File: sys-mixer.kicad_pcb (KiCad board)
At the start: 2 copper layers, 122 x 84 mm, 16 parts, among them J1 RCA L&R, J2 RCA L&R, J3 RCA L&R, SW1 4PDT

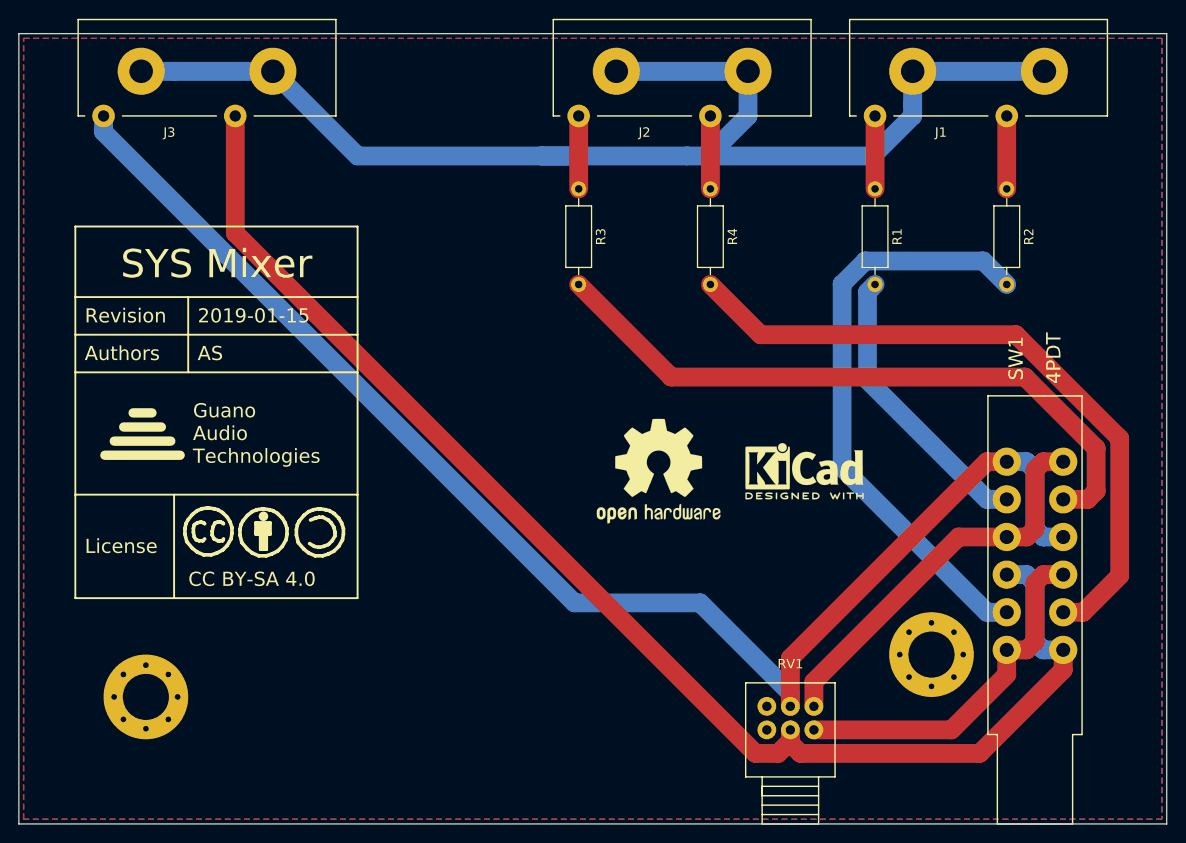
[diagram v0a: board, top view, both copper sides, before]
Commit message: Add github URL to silkscreen
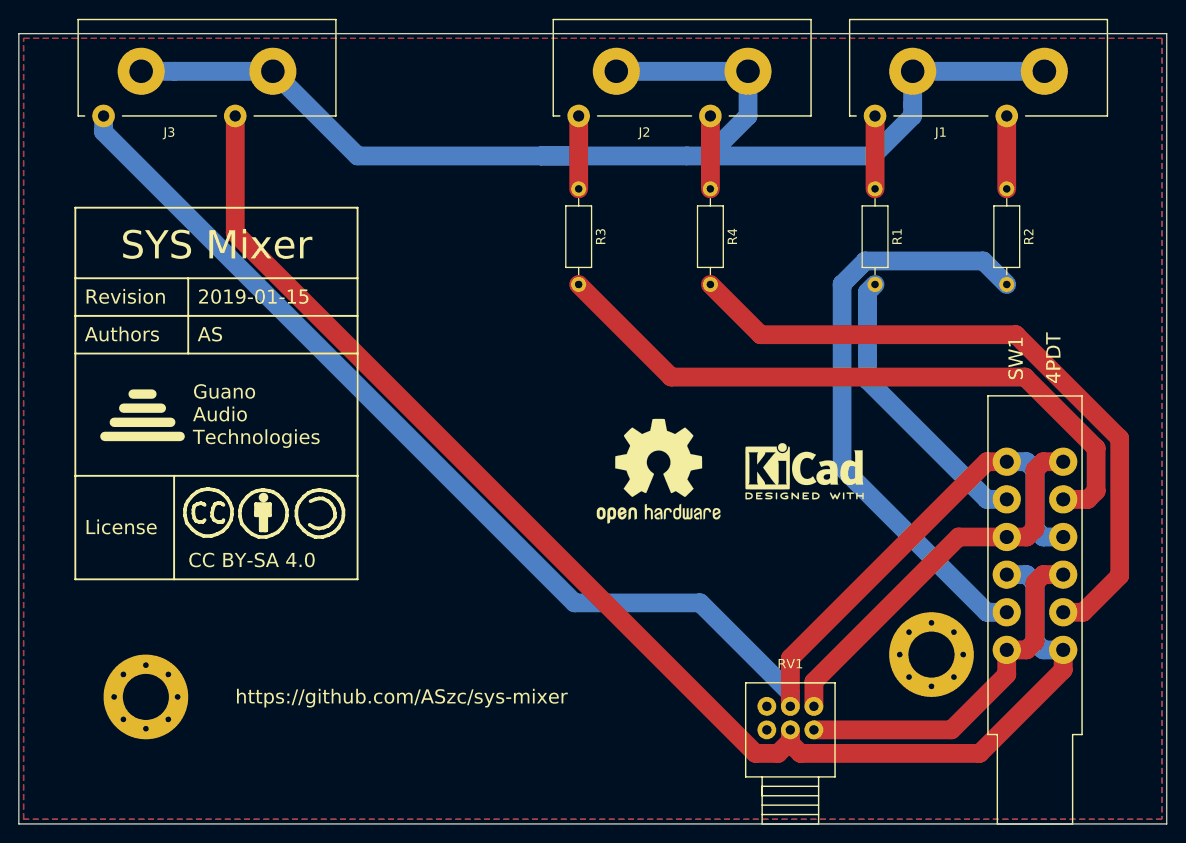
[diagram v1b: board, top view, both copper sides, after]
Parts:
- moved ? 2.00 mm to (70.0, 76.0)
- moved ? 2.00 mm to (76.0, 76.0)
- moved ? 2.00 mm to (82.0, 76.0)
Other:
- board text added: "https://github.com/ASzc/sys-mixer"
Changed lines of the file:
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@@
   (general
     (thickness 1.6)
-    (drawings 28)
+    (drawings 29)
     (tracks 88)
     (zones 0)
@@
   )
   (module extra-footprints:Symbol_CreativeCommons_Silkscreen_Type2_Small (layer F.Cu)
-    (at 70 78)
+    (at 70 76)
     (descr "Symbol, Creative Commons, Silkscreen, Type 2, Small,")
     (tags "Symbol, Creative Commons, Silkscreen, Type 2, Small,")
@@
   )
   (module extra-footprints:Symbol_CC-Attribution_Silkscreen_Small (layer F.Cu)
-    (at 76 78)
+    (at 76 76)
     (descr "Symbol, CC-Share Alike, Silkscreen, Small,")
     (tags "Symbol, CC-Share Alike, Silkscreen, Small,")
@@
   )
   (module extra-footprints:Symbol_CC-ShareAlike_Silkscreen_Small (layer F.Cu)
-    (at 82 78)
+    (at 82 76)
     (descr "Symbol, CC-Share Alike, Silkscreen, Small,")
     (tags "Symbol, CC-Share Alike, Silkscreen, Small,")
@@
     (fp_line (start -1.09982 1.19888) (end -0.59944 1.50114) (layer F.SilkS) (width 0.381))
   )
-  (gr_line (start 56 57) (end 86 57) (layer F.SilkS) (width 0.2))
-  (gr_line (start 56 61) (end 86 61) (layer F.SilkS) (width 0.2))
-  (gr_text Authors (at 57 59) (layer F.SilkS)
+  (gr_text https://github.com/ASzc/sys-mixer (at 73 95.5) (layer F.SilkS)
     (effects (font (size 1.5 1.5) (thickness 0.3)) (justify left))
   )
-  (gr_text AS (at 69 59) (layer F.SilkS)
+  (gr_line (start 56 55) (end 86 55) (layer F.SilkS) (width 0.2))
+  (gr_line (start 56 59) (end 86 59) (layer F.SilkS) (width 0.2))
+  (gr_text Authors (at 57 57) (layer F.SilkS)
     (effects (font (size 1.5 1.5) (thickness 0.3)) (justify left))
   )
-  (gr_text "CC BY-SA 4.0" (at 68 83) (layer F.SilkS)
+  (gr_text AS (at 69 57) (layer F.SilkS)
     (effects (font (size 1.5 1.5) (thickness 0.3)) (justify left))
   )
-  (gr_line (start 66.5 74) (end 66.5 85) (layer F.SilkS) (width 0.2))
-  (gr_line (start 86 85) (end 86 74) (layer F.SilkS) (width 0.2))
-  (gr_line (start 56 85) (end 86 85) (layer F.SilkS) (width 0.2))
-  (gr_line (start 56 74) (end 56 85) (layer F.SilkS) (width 0.2))
-  (gr_text License (at 57 79.5) (layer F.SilkS)
+  (gr_text "CC BY-SA 4.0" (at 68 81) (layer F.SilkS)
     (effects (font (size 1.5 1.5) (thickness 0.3)) (justify left))
   )
-  (gr_line (start 68 53) (end 68 61) (layer F.SilkS) (width 0.2))
-  (gr_line (start 86 53) (end 56 53) (layer F.SilkS) (width 0.2))
-  (gr_line (start 86 45.5) (end 56 45.5) (layer F.SilkS) (width 0.2))
-  (gr_line (start 86 74) (end 86 45.5) (layer F.SilkS) (width 0.2))
-  (gr_line (start 56 74) (end 86 74) (layer F.SilkS) (width 0.2))
-  (gr_line (start 56 45.5) (end 56 74) (layer F.SilkS) (width 0.2))
-  (gr_text 2019-01-15 (at 69 55) (layer F.SilkS)
+  (gr_line (start 66.5 72) (end 66.5 83) (layer F.SilkS) (width 0.2))
+  (gr_line (start 86 83) (end 86 72) (layer F.SilkS) (width 0.2))
+  (gr_line (start 56 83) (end 86 83) (layer F.SilkS) (width 0.2))
+  (gr_line (start 56 72) (end 56 83) (layer F.SilkS) (width 0.2))
+  (gr_text License (at 57 77.5) (layer F.SilkS)
     (effects (font (size 1.5 1.5) (thickness 0.3)) (justify left))
   )
-  (gr_text Revision (at 57 55) (layer F.SilkS)
+  (gr_line (start 68 51) (end 68 59) (layer F.SilkS) (width 0.2))
+  (gr_line (start 86 51) (end 56 51) (layer F.SilkS) (width 0.2))
+  (gr_line (start 86 43.5) (end 56 43.5) (layer F.SilkS) (width 0.2))
+  (gr_line (start 86 72) (end 86 43.5) (layer F.SilkS) (width 0.2))
+  (gr_line (start 56 72) (end 86 72) (layer F.SilkS) (width 0.2))
+  (gr_line (start 56 43.5) (end 56 72) (layer F.SilkS) (width 0.2))
+  (gr_text 2019-01-15 (at 69 53) (layer F.SilkS)
     (effects (font (size 1.5 1.5) (thickness 0.3)) (justify left))
   )
-  (gr_text "SYS Mixer" (at 71 49.5) (layer F.SilkS)
+  (gr_text Revision (at 57 53) (layer F.SilkS)
+    (effects (font (size 1.5 1.5) (thickness 0.3)) (justify left))
+  )
+  (gr_text "SYS Mixer" (at 71 47.5) (layer F.SilkS)
     (effects (font (size 3 3) (thickness 0.5)))
   )
-  (gr_line (start 64.142965 65.310602) (end 62.142965 65.310602) (layer F.SilkS) (width 1))
-  (gr_line (start 65.142965 66.810602) (end 61.142965 66.810602) (layer F.SilkS) (width 1))
-  (gr_line (start 66.142965 68.310602) (end 60.142965 68.310602) (layer F.SilkS) (width 1))
-  (gr_line (start 67.142965 69.810602) (end 59.142965 69.810602) (layer F.SilkS) (width 1))
-  (gr_text "Guano\nAudio\nTechnologies" (at 68.5 67.5) (layer F.SilkS)
+  (gr_line (start 64.142965 63.310602) (end 62.142965 63.310602) (layer F.SilkS) (width 1))
+  (gr_line (start 65.142965 64.810602) (end 61.142965 64.810602) (layer F.SilkS) (width 1))
+  (gr_line (start 66.142965 66.310602) (end 60.142965 66.310602) (layer F.SilkS) (width 1))
+  (gr_line (start 67.142965 67.810602) (end 59.142965 67.810602) (layer F.SilkS) (width 1))
+  (gr_text "Guano\nAudio\nTechnologies" (at 68.5 65.5) (layer F.SilkS)
     (effects (font (size 1.5 1.5) (thickness 0.3)) (justify left))
   )
@@
   (gr_line (start 172 25) (end 172 109) (layer Edge.Cuts) (width 0.01))
   (gr_line (start 50 25) (end 172 25) (layer Edge.Cuts) (width 0.01))
-  (segment (start 66.535533 29) (end 77 29) (width 2) (layer B.Cu) (net 13))
-  (segment (start 63 29) (end 66.535533 29) (width 2) (layer B.Cu) (net 13))
-  (segment (start 77 29) (end 86 38) (width 2) (layer B.Cu) (net 13))
-  (segment (start 145 32.535533) (end 145 29) (width 2) (layer B.Cu) (net 13))
-  (segment (start 145 33.746002) (end 145 32.535533) (width 2) (layer B.Cu) (net 13))
-  (segment (start 140.746002 38) (end 145 33.746002) (width 2) (layer B.Cu) (net 13))
-  (segment (start 123.246002 38) (end 140.746002 38) (width 2) (layer B.Cu) (net 13))
-  (segment (start 113.5 29) (end 127.5 29) (width 2) (layer B.Cu) (net 13))
-  (segment (start 145 29) (end 159 29) (width 2) (layer B.Cu) (net 13))
-  (segment (start 109.246002 38) (end 105.5 38) (width 2) (layer B.Cu) (net 13))
-  (segment (start 123.246002 38) (end 121 38) (width 2) (layer B.Cu) (net 13))
-  (segment (start 127.5 29) (end 127.5 33.746002) (width 2) (layer B.Cu) (net 13))
-  (segment (start 127.5 33.746002) (end 123.246002 38) (width 2) (layer B.Cu) (net 13))
-  (segment (start 105.5 38) (end 121 38) (width 2) (layer B.Cu) (net 13))
   (segment (start 141 33.75) (end 141 41.5) (width 2) (layer F.Cu) (net 1))
   (segment (start 155 33.75) (end 155 41.5) (width 2) (layer F.Cu) (net 2))
@@
   (segment (start 152.499991 49.159991) (end 139.964461 49.159991) (width 2) (layer B.Cu) (net 8))
   (segment (start 155 51.66) (end 152.499991 49.159991) (width 2) (layer B.Cu) (net 8))
-  (segment (start 161.059998 86.5) (end 161.5 86.5) (width 2) (layer F.Cu) (net 10))
   (segment (start 161.059998 74.5) (end 161.5 74.5) (width 2) (layer B.Cu) (net 9))
   (segment (start 164.500001 69.059999) (end 164.500001 73.621319) (width 2) (layer F.Cu) (net 9))
@@
   (segment (start 163.62132 74.5) (end 161 74.5) (width 2) (layer F.Cu) (net 9))
   (segment (start 164.500001 73.621319) (end 163.62132 74.5) (width 2) (layer F.Cu) (net 9))
+  (segment (start 161.059998 86.5) (end 161.5 86.5) (width 2) (layer F.Cu) (net 10))
   (segment (start 163.12132 86.5) (end 161 86.5) (width 2) (layer F.Cu) (net 10))
   (segment (start 167.000011 82.621309) (end 163.12132 86.5) (width 2) (layer F.Cu) (net 10))
@@
   (segment (start 158 77.62132) (end 158 71.37868) (width 2) (layer F.Cu) (net 12))
   (segment (start 155 78.5) (end 157.12132 78.5) (width 2) (layer F.Cu) (net 12))
+  (segment (start 66.535533 29) (end 77 29) (width 2) (layer B.Cu) (net 13))
+  (segment (start 63 29) (end 66.535533 29) (width 2) (layer B.Cu) (net 13))
+  (segment (start 77 29) (end 86 38) (width 2) (layer B.Cu) (net 13))
+  (segment (start 145 32.535533) (end 145 29) (width 2) (layer B.Cu) (net 13))
+  (segment (start 145 33.746002) (end 145 32.535533) (width 2) (layer B.Cu) (net 13))
+  (segment (start 140.746002 38) (end 145 33.746002) (width 2) (layer B.Cu) (net 13))
+  (segment (start 123.246002 38) (end 140.746002 38) (width 2) (layer B.Cu) (net 13))
+  (segment (start 113.5 29) (end 127.5 29) (width 2) (layer B.Cu) (net 13))
+  (segment (start 145 29) (end 159 29) (width 2) (layer B.Cu) (net 13))
+  (segment (start 109.246002 38) (end 105.5 38) (width 2) (layer B.Cu) (net 13))
+  (segment (start 123.246002 38) (end 121 38) (width 2) (layer B.Cu) (net 13))
+  (segment (start 127.5 29) (end 127.5 33.746002) (width 2) (layer B.Cu) (net 13))
+  (segment (start 127.5 33.746002) (end 123.246002 38) (width 2) (layer B.Cu) (net 13))
+  (segment (start 105.5 38) (end 121 38) (width 2) (layer B.Cu) (net 13))
   (segment (start 86 38) (end 105.5 38) (width 2) (layer B.Cu) (net 13))
   (zone (net 13) (net_name "Net-(H1-Pad1)") (layer F.Cu) (hatch edge 0.508)

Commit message: Reroute output so both channels are on B.Cu
Also adjust silk info position
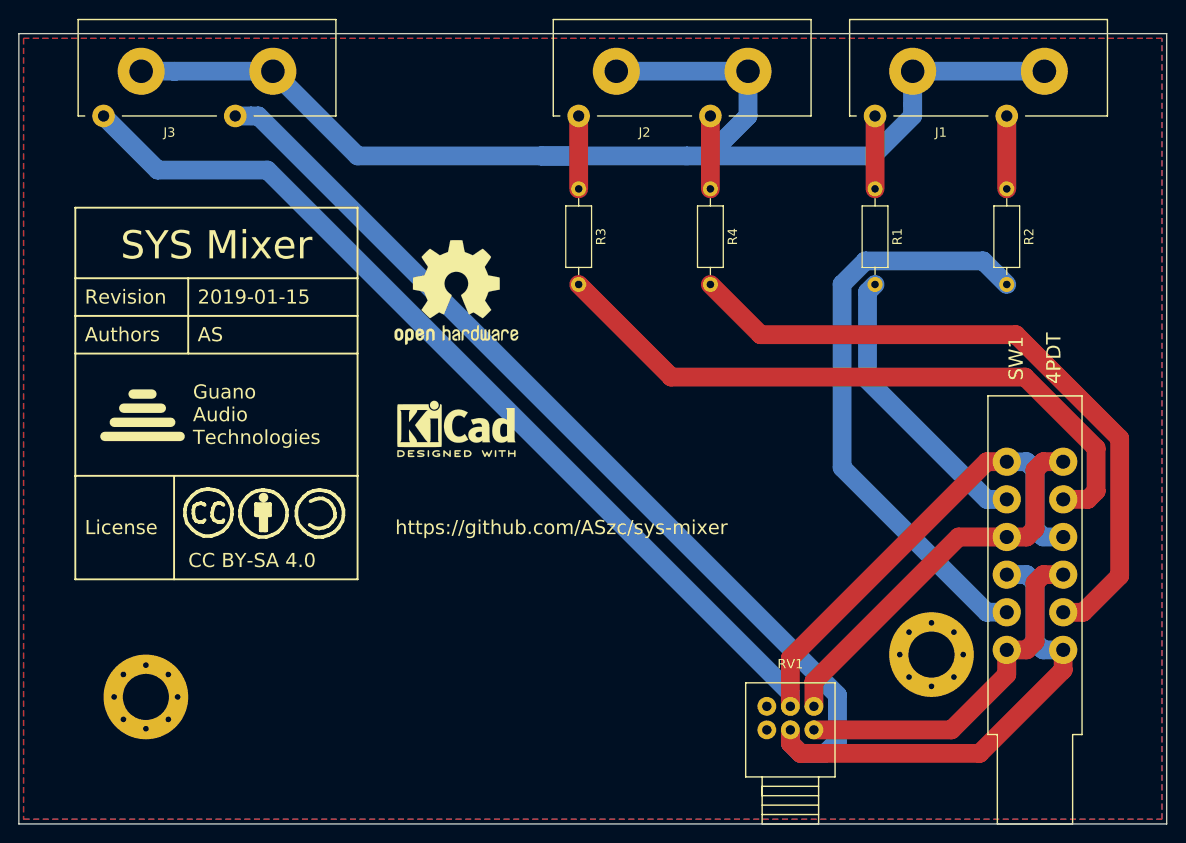
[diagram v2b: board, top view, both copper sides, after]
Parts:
- moved REF** 37.3 mm to (96.5, 67.0)
- moved REF** 28.7 mm to (96.5, 52.5)
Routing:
- net Net-(J3-Pad2): track 145.0 -> 151.9 mm
- net Net-(J3-Pad1): track 150.6 -> 149.6 mm
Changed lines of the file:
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@@
     (thickness 1.6)
     (drawings 29)
-    (tracks 88)
+    (tracks 91)
     (zones 0)
     (modules 16)
@@
   )
   (module Symbol:KiCad-Logo2_6mm_SilkScreen (layer F.Cu)
-    (at 133.5 71.5)
+    (at 96.5 67)
     (descr "KiCad Logo")
     (tags "Logo KiCad")
@@
   )
   (module Symbol:OSHW-Logo2_14.6x12mm_SilkScreen (layer F.Cu)
-    (at 118 71.5)
+    (at 96.5 52.5)
     (descr "Open Source Hardware Symbol")
     (tags "Logo Symbol OSHW")
@@
     (fp_line (start -1.09982 1.19888) (end -0.59944 1.50114) (layer F.SilkS) (width 0.381))
   )
-  (gr_text https://github.com/ASzc/sys-mixer (at 73 95.5) (layer F.SilkS)
+  (gr_text https://github.com/ASzc/sys-mixer (at 90 77.5) (layer F.SilkS)
     (effects (font (size 1.5 1.5) (thickness 0.3)) (justify left))
   )
@@
   (segment (start 123.5 33.75) (end 123.5 41.5) (width 2) (layer F.Cu) (net 3))
   (segment (start 109.5 33.75) (end 109.5 41.5) (width 2) (layer F.Cu) (net 4))
-  (segment (start 59 35.447056) (end 109.052944 85.5) (width 2) (layer B.Cu) (net 5))
-  (segment (start 59 33.75) (end 59 35.447056) (width 2) (layer B.Cu) (net 5))
   (segment (start 132 95.085787) (end 132 96.5) (width 2) (layer B.Cu) (net 5))
-  (segment (start 122.414213 85.5) (end 132 95.085787) (width 2) (layer B.Cu) (net 5))
-  (segment (start 109.052944 85.5) (end 122.414213 85.5) (width 2) (layer B.Cu) (net 5))
   (segment (start 152.87868 70.5) (end 155 70.5) (width 2) (layer F.Cu) (net 5))
   (segment (start 132 91.37868) (end 152.87868 70.5) (width 2) (layer F.Cu) (net 5))
@@
   (segment (start 158.87868 78.5) (end 158 77.62132) (width 2) (layer B.Cu) (net 5))
   (segment (start 161 78.5) (end 158.87868 78.5) (width 2) (layer B.Cu) (net 5))
-  (segment (start 130.700001 101.500001) (end 132 100.200002) (width 2) (layer F.Cu) (net 6))
-  (segment (start 128.299999 101.500001) (end 130.700001 101.500001) (width 2) (layer F.Cu) (net 6))
-  (segment (start 73 46.200002) (end 128.299999 101.500001) (width 2) (layer F.Cu) (net 6))
-  (segment (start 73 33.75) (end 73 46.200002) (width 2) (layer F.Cu) (net 6))
+  (segment (start 132 95.085787) (end 76.414213 39.5) (width 2) (layer B.Cu) (net 5))
+  (segment (start 64.75 39.5) (end 59 33.75) (width 2) (layer B.Cu) (net 5))
+  (segment (start 76.414213 39.5) (end 64.75 39.5) (width 2) (layer B.Cu) (net 5))
   (segment (start 132 100.414213) (end 133.085797 101.50001) (width 2) (layer F.Cu) (net 6))
   (segment (start 132 99) (end 132 100.414213) (width 2) (layer F.Cu) (net 6))
@@
   (segment (start 152.12131 101.50001) (end 161 92.62132) (width 2) (layer F.Cu) (net 6))
   (segment (start 133.085797 101.50001) (end 152.12131 101.50001) (width 2) (layer F.Cu) (net 6))
+  (segment (start 74.697056 33.75) (end 73 33.75) (width 2) (layer B.Cu) (net 6))
+  (segment (start 75.450002 33.75) (end 74.697056 33.75) (width 2) (layer B.Cu) (net 6))
+  (segment (start 137.000001 95.299999) (end 75.450002 33.75) (width 2) (layer B.Cu) (net 6))
+  (segment (start 137.000001 100.200001) (end 137.000001 95.299999) (width 2) (layer B.Cu) (net 6))
+  (segment (start 135.700001 101.500001) (end 137.000001 100.200001) (width 2) (layer B.Cu) (net 6))
+  (segment (start 133.085788 101.500001) (end 135.700001 101.500001) (width 2) (layer B.Cu) (net 6))
+  (segment (start 132 100.414213) (end 133.085788 101.500001) (width 2) (layer B.Cu) (net 6))
+  (segment (start 132 99) (end 132 100.414213) (width 2) (layer B.Cu) (net 6))
   (segment (start 152.87868 74.5) (end 155 74.5) (width 2) (layer B.Cu) (net 7))
   (segment (start 140.200001 61.821321) (end 152.87868 74.5) (width 2) (layer B.Cu) (net 7))
@@
     (polygon
       (pts
-        (xy 50.5 25.5) (xy 171.5 25.5) (xy 171.5 108.5) (xy 50.5 108.5)
+        (xy 50.5 25.5) (xy 50.5 108.5) (xy 171.5 108.5) (xy 171.5 25.5)
       )
     )
@@
     (polygon
       (pts
-        (xy 50.5 25.5) (xy 171.5 25.5) (xy 171.5 108.5) (xy 50.5 108.5)
+        (xy 50.5 25.5) (xy 50.5 108.5) (xy 171.5 108.5) (xy 171.5 25.5)
       )
     )
